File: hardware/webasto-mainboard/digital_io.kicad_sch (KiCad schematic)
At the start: 35 parts, among them Q10 DMG2301L, Q2 2N7002, Q3 2N7002, Q4 2N7002, Q5 2N7002, Q6 SUD50P04-08, Q7 SUD50P04-08, Q8 SUD50P04-08, Q9 SUD50P04-08, U4 MC33660BEFR2

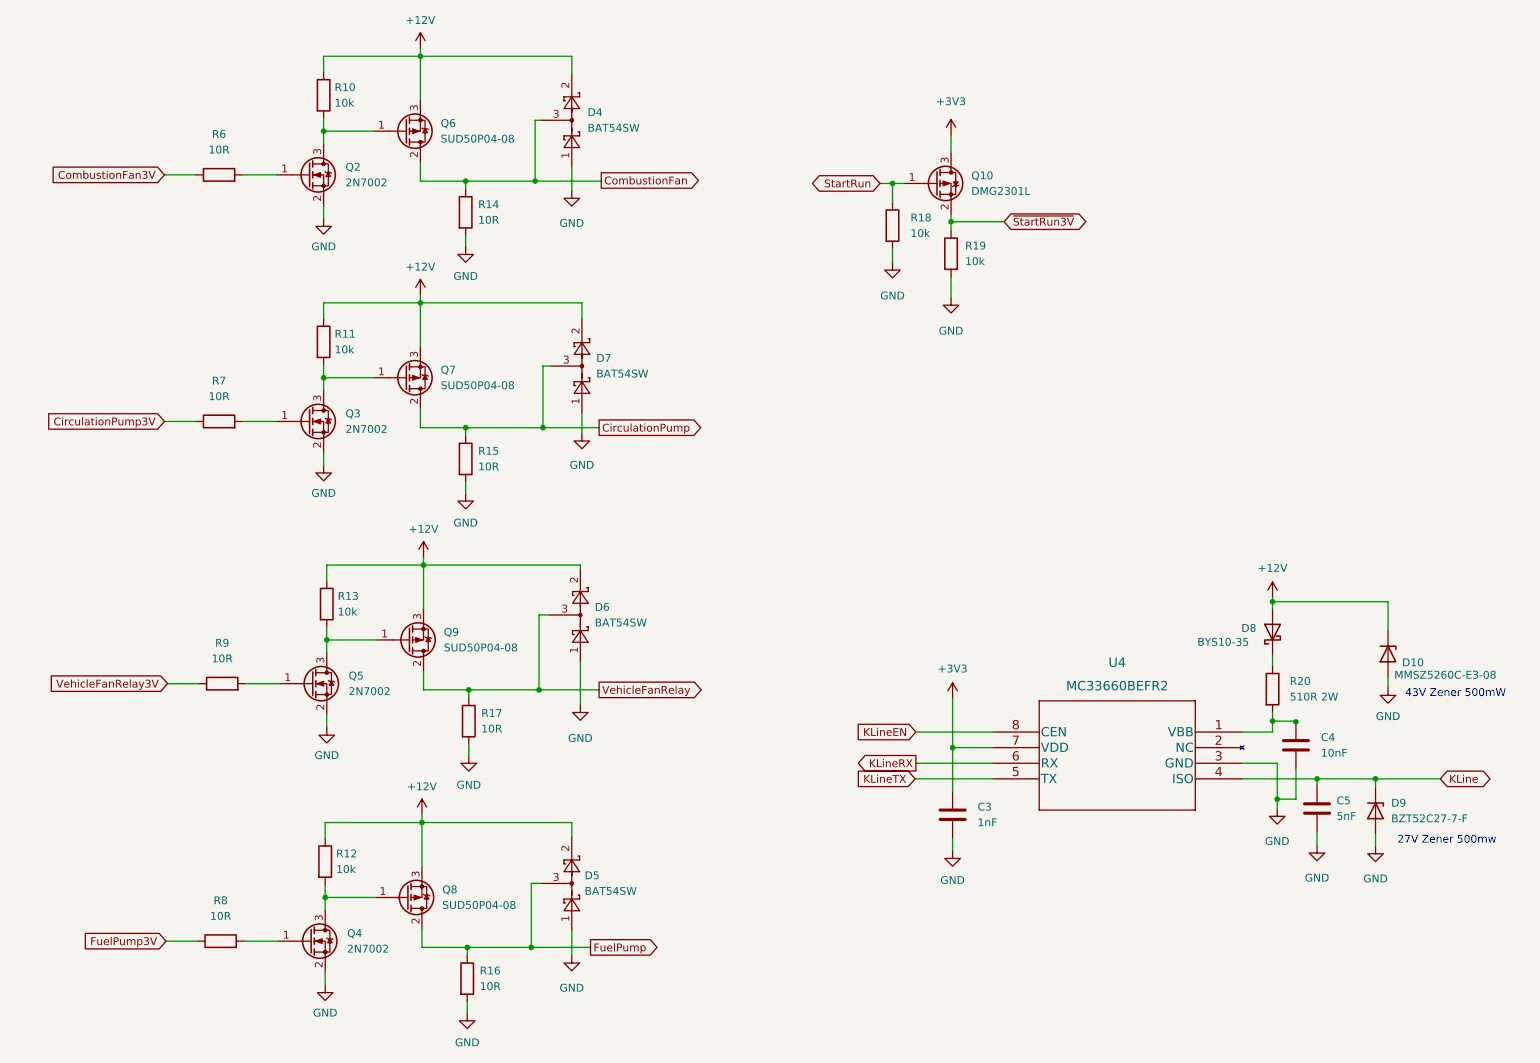
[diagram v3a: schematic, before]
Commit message: Move start/run to sensor board, add CANBUS
- WiFi is not being very helpful, and I'm concerned it won't work well once
  installed in the bus...  CANBus wiring is easy.
- Removed both Start/Run and the Vehicle Fan Relay from X1 to make space for
  canbus
- moved LEDs onto an I2C gpio extender.
- will need to still plumb in CAN_EN support
- will also need to yank out the WiFi stuff that won't stay stable anyways
  and reroute the CBOR out the CANBus instead of WiFi
- Vehicle Fan control will need to move to a LINBus fan controller board
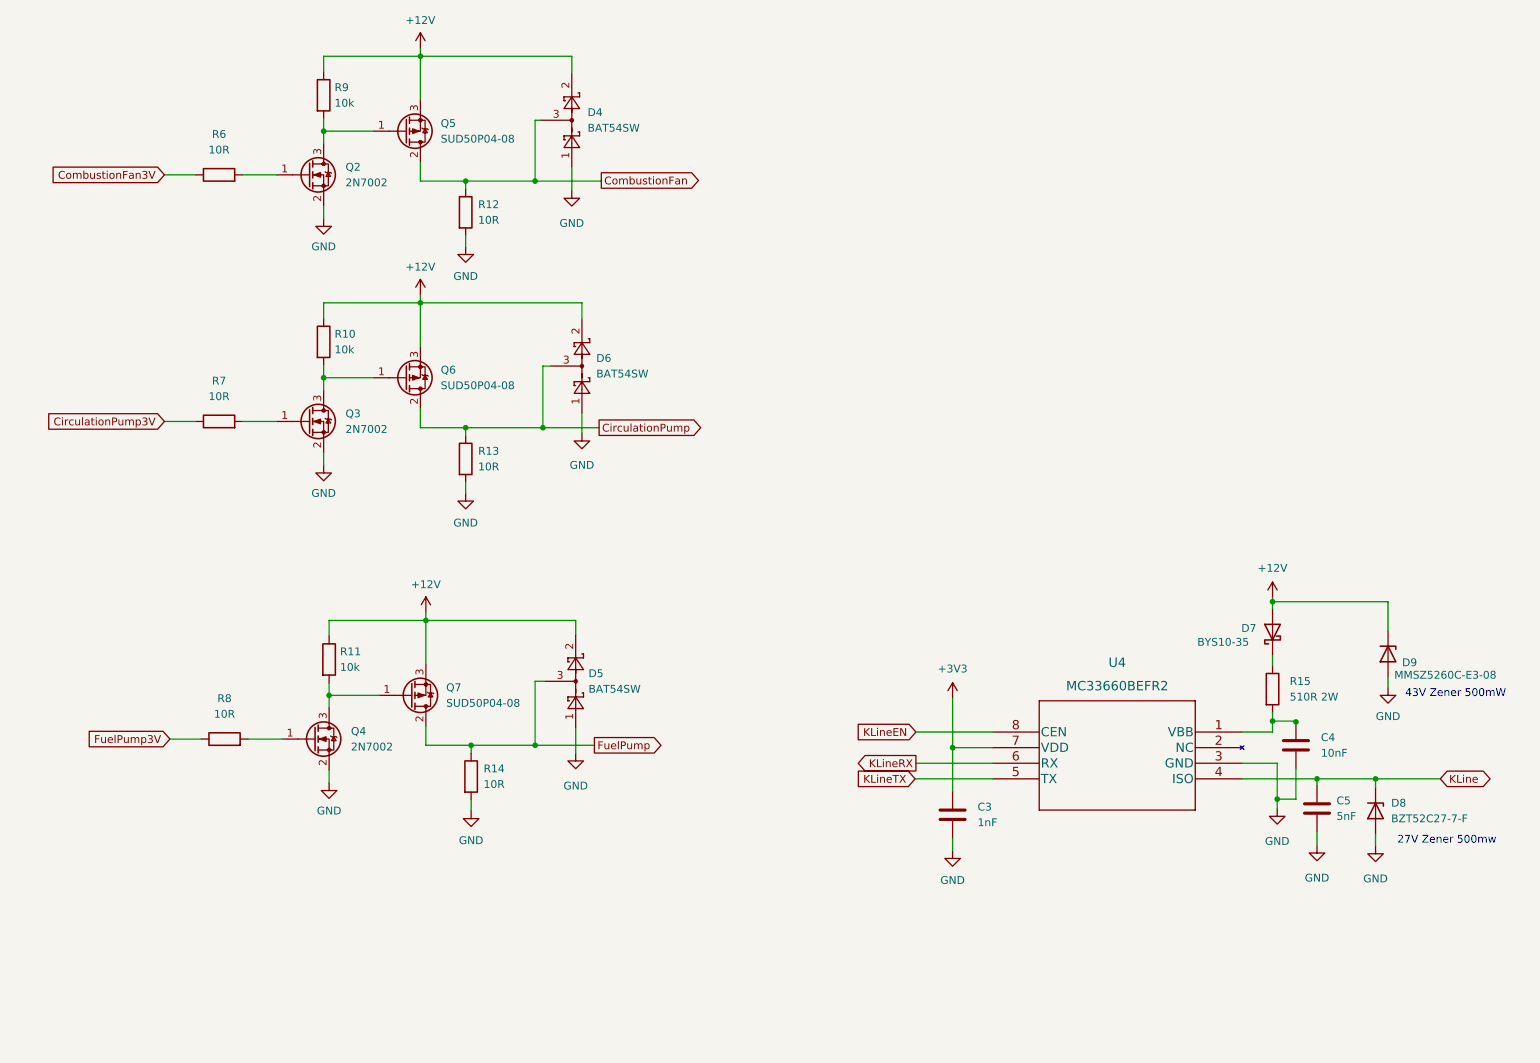
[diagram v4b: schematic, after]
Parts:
- removed D6: BAT54SW, Package_TO_SOT_SMD:SOT-323_SC-70, symbol Diode:BAT54SW
- removed Q10: DMG2301L, Package_TO_SOT_SMD:SOT-23, symbol Transistor_FET:DMG2301L
- removed Q5: 2N7002, Package_TO_SOT_SMD:SOT-23, symbol Transistor_FET:2N7002
- removed Q9: SUD50P04-08, Package_TO_SOT_SMD:TO-252-2, symbol Transistor_FET:SUD50P04-08
- removed R13, R18, R19: 10k, Resistor_SMD:R_0805_2012Metric_Pad1.20x1.40mm_HandSolder, symbol Device:R
- removed R17, R9: 10R, Resistor_SMD:R_0805_2012Metric_Pad1.20x1.40mm_HandSolder, symbol Device:R
- renumbered D7 to D6, D8 to D7, D9 to D8, D10 to D9, Q6 to Q5, Q7 to Q6, Q8 to Q7, R11 to R10, R12 to R11, R14 to R12, R15 to R13, R16 to R14, R20 to R15, R10 to R9
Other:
- moved on the sheet: D5, Q4, Q7, R11, R14, R8

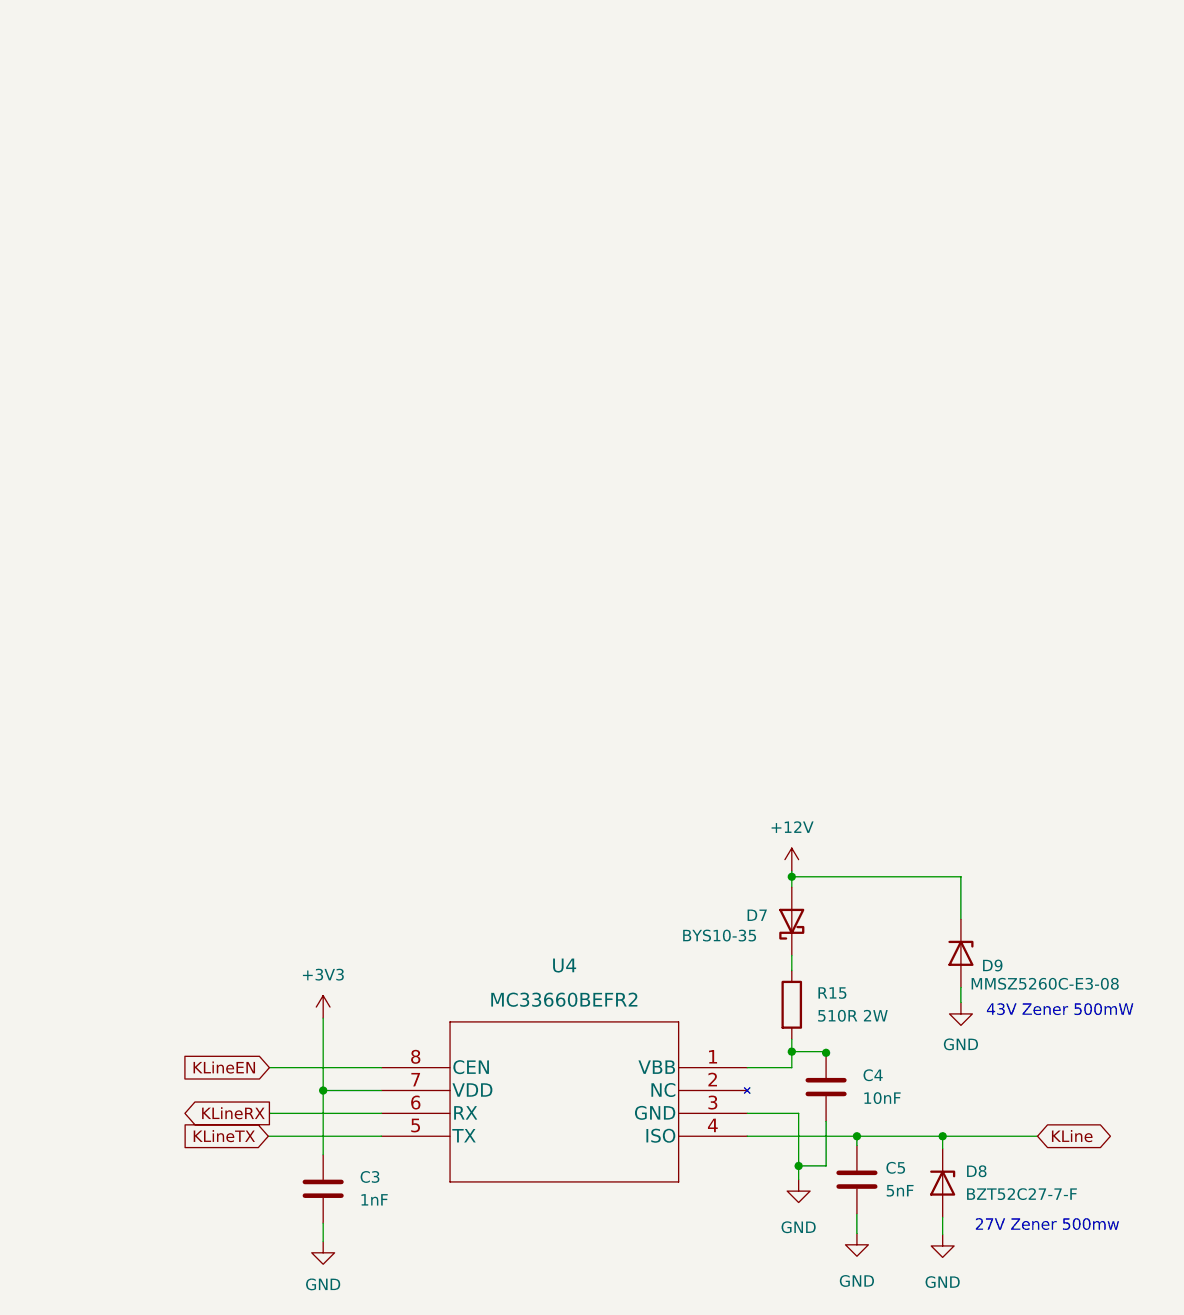
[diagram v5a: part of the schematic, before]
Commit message: Removing KLine and I2C from X1, reattaching the external IOs.
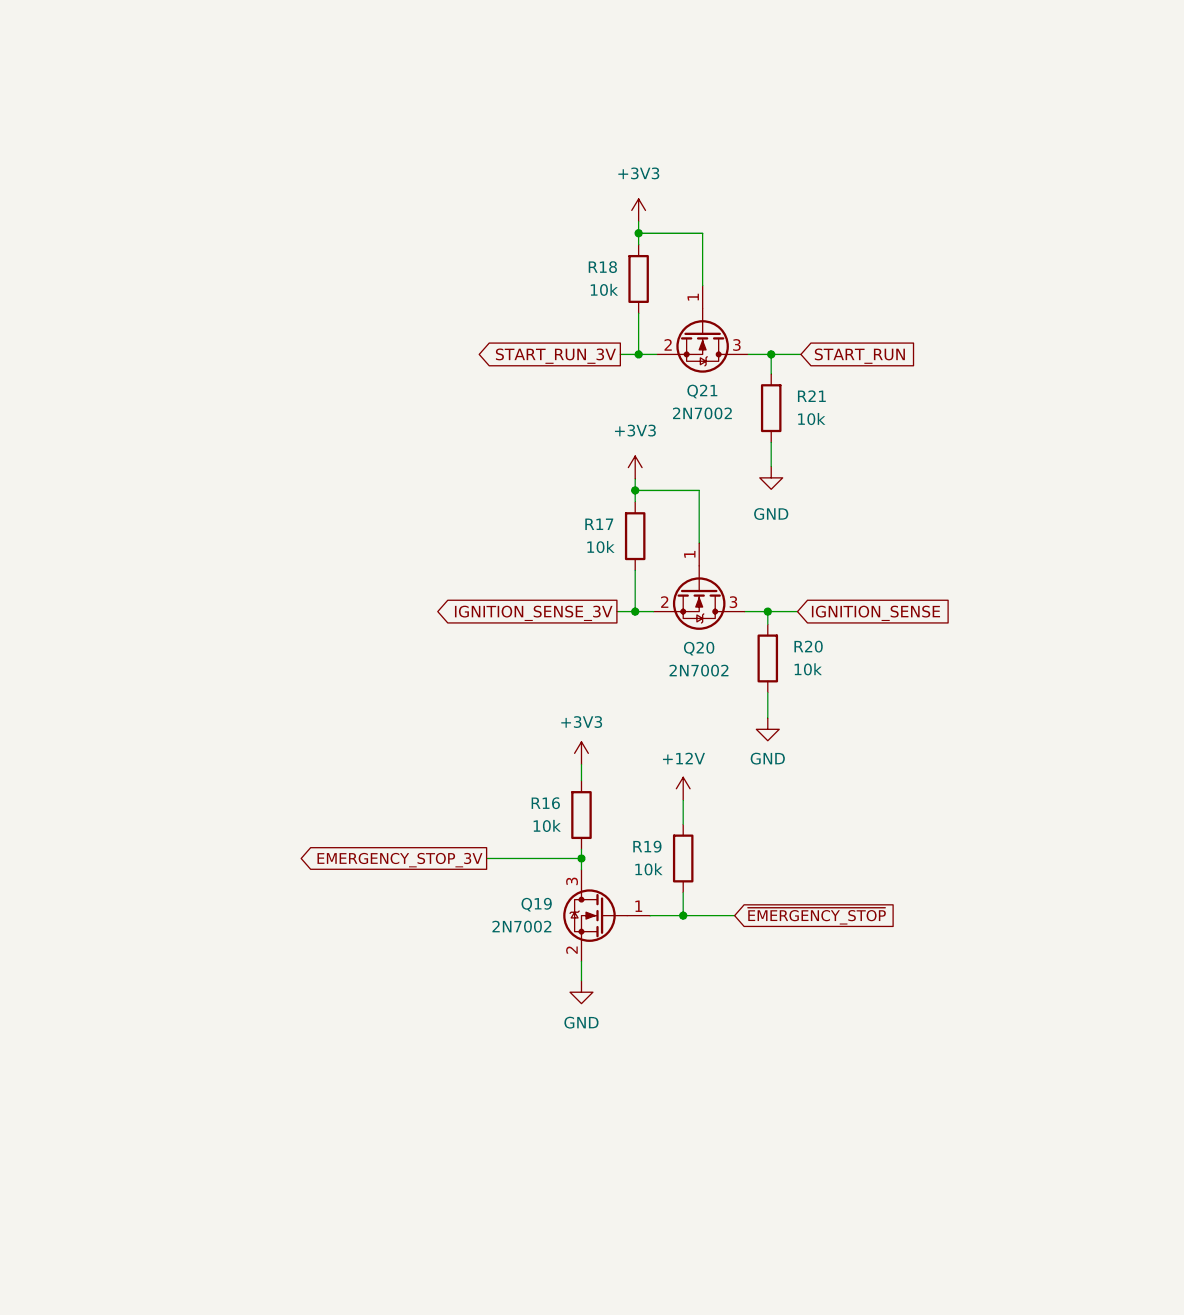
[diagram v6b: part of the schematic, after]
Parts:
- removed C3: 1nF, Capacitor_SMD:C_0805_2012Metric, symbol Device:C
- removed C4: 10nF, Capacitor_SMD:C_0805_2012Metric, symbol Device:C
- removed C5: 5nF, Capacitor_SMD:C_0805_2012Metric, symbol Device:C
- removed D7: BYS10-35, Diode_SMD:D_SMA_Handsoldering, symbol Device:D_Schottky
- removed D8: BZT52C27-7-F, Diode_SMD:D_SOD-123, symbol Device:D_Zener
- removed D9: MMSZ5260C-E3-08, Diode_SMD:D_SOD-123, symbol Device:D_Zener
- removed R15: 510R 2W, Resistor_SMD:R_2512_6332Metric_Pad1.40x3.35mm_HandSolder, symbol Device:R
- removed U4: MC33660BEFR2, UltraLibrarian:MC33660BEFR2, symbol UltraLibrarian:MC33660BEFR2
- added Q19, Q20, Q21: 2N7002, Package_TO_SOT_SMD:SOT-23, symbol Transistor_FET:2N7002
- added R16, R17, R18, R19, R20, R21: 10k, Resistor_SMD:R_0805_2012Metric_Pad1.20x1.40mm_HandSolder, symbol Device:R
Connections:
- net +12V: now also R19.2
- net +3V3: now also Q20.1 (G), Q21.1 (G), R16.2, R17.2, R18.2
- net GND: now also Q19.2 (S), R20.1, R21.1
- new net EMERGENCY_STOP_3V: Q19.3 (D), R16.1
- new net IGNITION_SENSE: Q20.3 (D), R20.2
- new net IGNITION_SENSE_3V: Q20.2 (S), R17.1
- new net START_RUN: Q21.3 (D), R21.2
- new net START_RUN_3V: Q21.2 (S), R18.1
- new net ~{EMERGENCY_STOP}: Q19.1 (G), R19.1
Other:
- note removed: "27V Zener 500mw"
- note removed: "43V Zener 500mW"
